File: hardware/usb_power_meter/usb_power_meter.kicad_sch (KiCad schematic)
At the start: 43 parts, among them J1 KH-1.27PH180-2X5P-L7.2-SMT, J2 917-P81A202ES60201, J4 A/F LCPTrue color1.2pillar_C4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, Q1 2N7002, Q2 IRML6401, SW1 TS-1187A-B-A-B, U1 nRF52833-QDxx, U2 INA226, X1 32Mhz crystal, X2 32.768kHz crystal

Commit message: Fix via sizes and 10k resistor footprint
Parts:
- R2, R3, R5, R6, R7: footprint Resistor_SMD:R_0201_0603Metric -> Resistor_SMD:R_0402_1005Metric; LCSC C25804 -> C270371
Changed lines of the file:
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@@
       (effects (font (size 1.27 1.27)) (justify left))
     )
-    (property "Footprint" "Resistor_SMD:R_0201_0603Metric" (at 139.7 137.668 90)
+    (property "Footprint" "Resistor_SMD:R_0402_1005Metric" (at 139.7 137.668 90)
       (effects (font (size 1.27 1.27)) hide)
     )
@@
       (effects (font (size 1.27 1.27)) hide)
     )
-    (property "LCSC" "C25804" (at 139.7 135.89 0)
+    (property "LCSC" "C270371" (at 139.7 135.89 0)
       (effects (font (size 1.27 1.27)) hide)
     )
@@
       (effects (font (size 1.27 1.27)) (justify left))
     )
-    (property "Footprint" "Resistor_SMD:R_0201_0603Metric" (at 144.78 147.828 90)
+    (property "Footprint" "Resistor_SMD:R_0402_1005Metric" (at 144.78 147.828 90)
       (effects (font (size 1.27 1.27)) hide)
     )
@@
       (effects (font (size 1.27 1.27)) hide)
     )
-    (property "LCSC" "C25804" (at 144.78 146.05 0)
+    (property "LCSC" "C270371" (at 144.78 146.05 0)
       (effects (font (size 1.27 1.27)) hide)
     )
@@
       (effects (font (size 1.27 1.27)) (justify left))
     )
-    (property "Footprint" "Resistor_SMD:R_0201_0603Metric" (at 75.692 181.61 90)
+    (property "Footprint" "Resistor_SMD:R_0402_1005Metric" (at 75.692 181.61 90)
       (effects (font (size 1.27 1.27)) hide)
     )
@@
       (effects (font (size 1.27 1.27)) hide)
     )
-    (property "LCSC" "C25804" (at 77.47 181.61 0)
+    (property "LCSC" "C270371" (at 77.47 181.61 0)
       (effects (font (size 1.27 1.27)) hide)
     )
@@
       (effects (font (size 1.27 1.27)) (justify left))
     )
-    (property "Footprint" "Resistor_SMD:R_0201_0603Metric" (at 92.202 167.64 90)
+    (property "Footprint" "Resistor_SMD:R_0402_1005Metric" (at 92.202 167.64 90)
       (effects (font (size 1.27 1.27)) hide)
     )
@@
       (effects (font (size 1.27 1.27)) hide)
     )
-    (property "LCSC" "C25804" (at 93.98 167.64 0)
+    (property "LCSC" "C270371" (at 93.98 167.64 0)
       (effects (font (size 1.27 1.27)) hide)
     )
@@
       (effects (font (size 1.27 1.27)) (justify left))
     )
-    (property "Footprint" "Resistor_SMD:R_0201_0603Metric" (at 142.24 142.748 90)
+    (property "Footprint" "Resistor_SMD:R_0402_1005Metric" (at 142.24 142.748 90)
       (effects (font (size 1.27 1.27)) hide)
     )
@@
       (effects (font (size 1.27 1.27)) hide)
     )
-    (property "LCSC" "C25804" (at 142.24 140.97 0)
-      (effects (font (size 1.27 1.27)) hide)
-    )
+    (property "LCSC" "C270371" (at 142.24 140.97 0)
+      (effects (font (size 1.27 1.27)) hide)
+    )

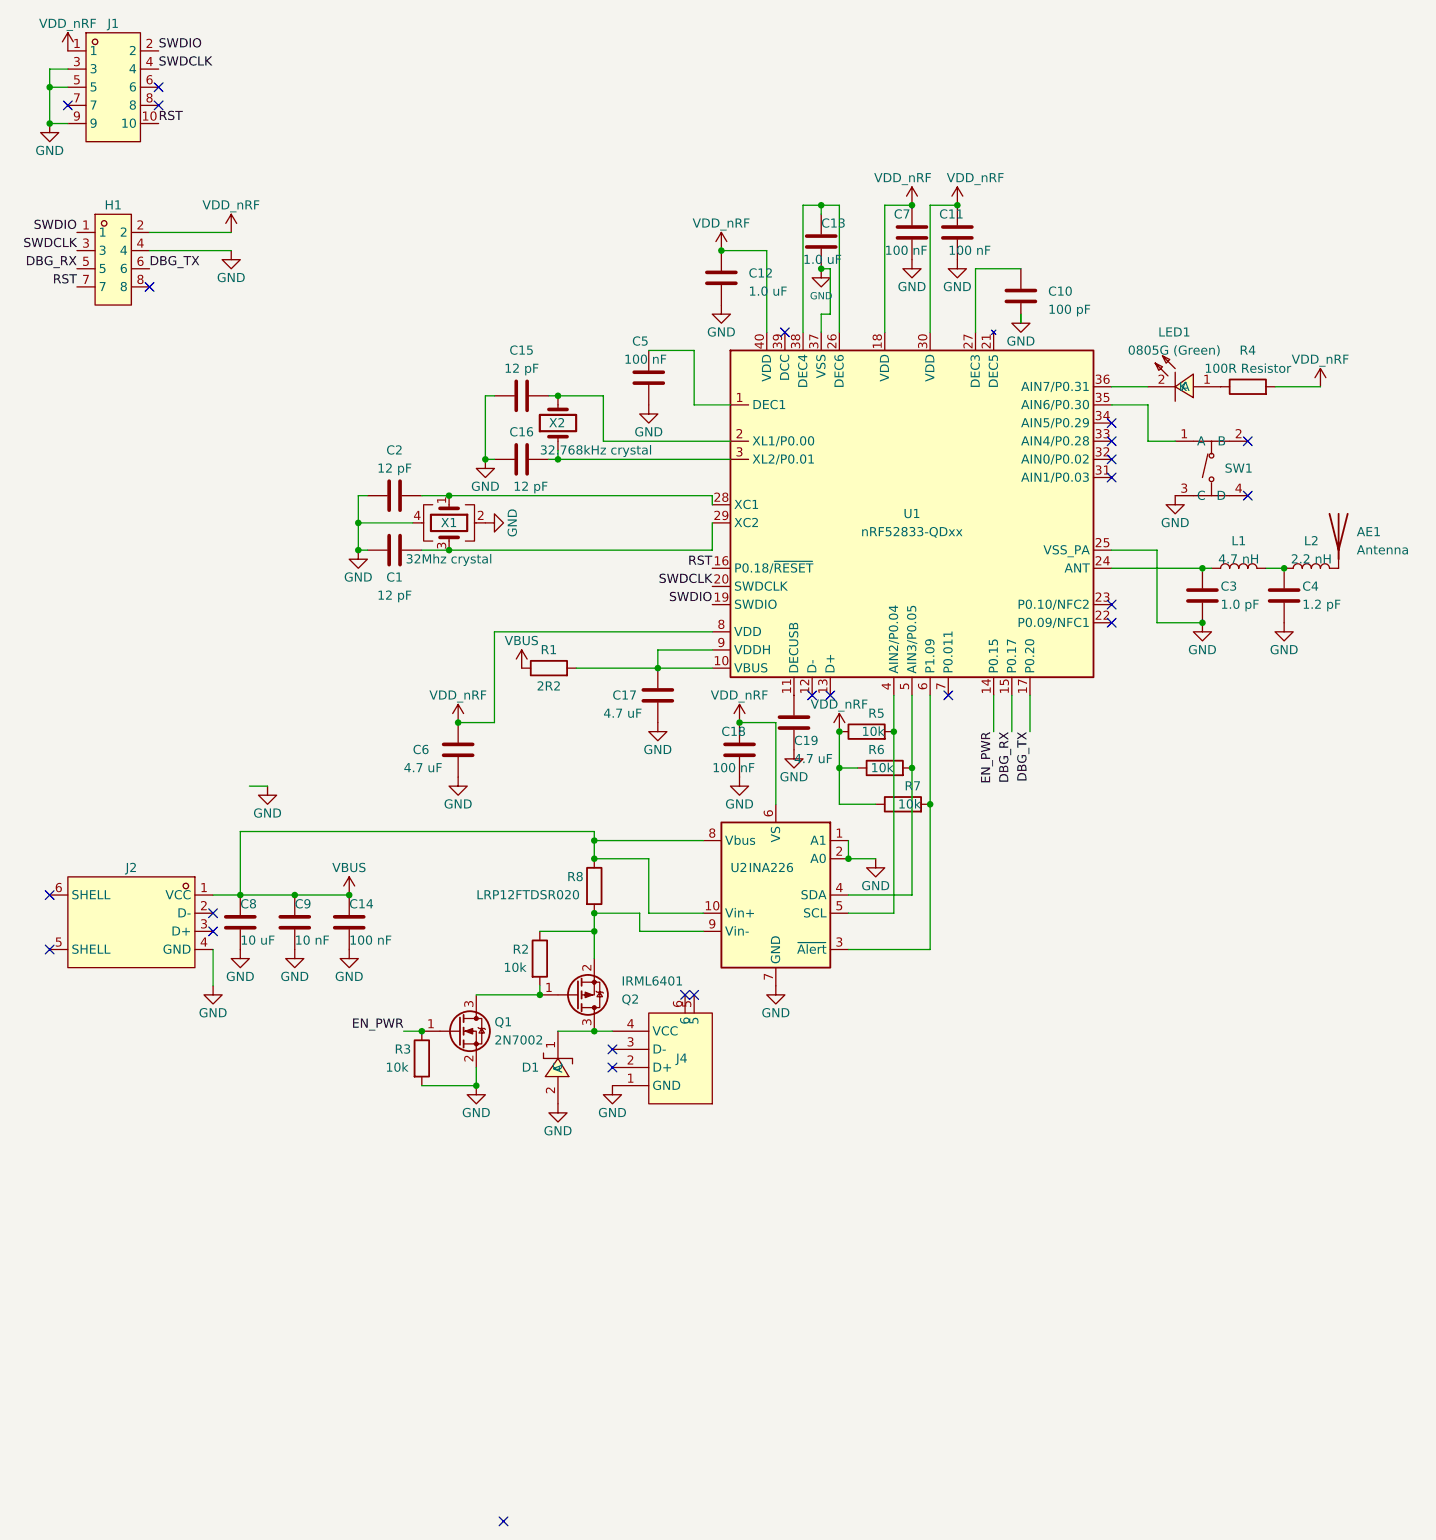
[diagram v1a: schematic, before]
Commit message: Update KiCad projects to the KiCad 8
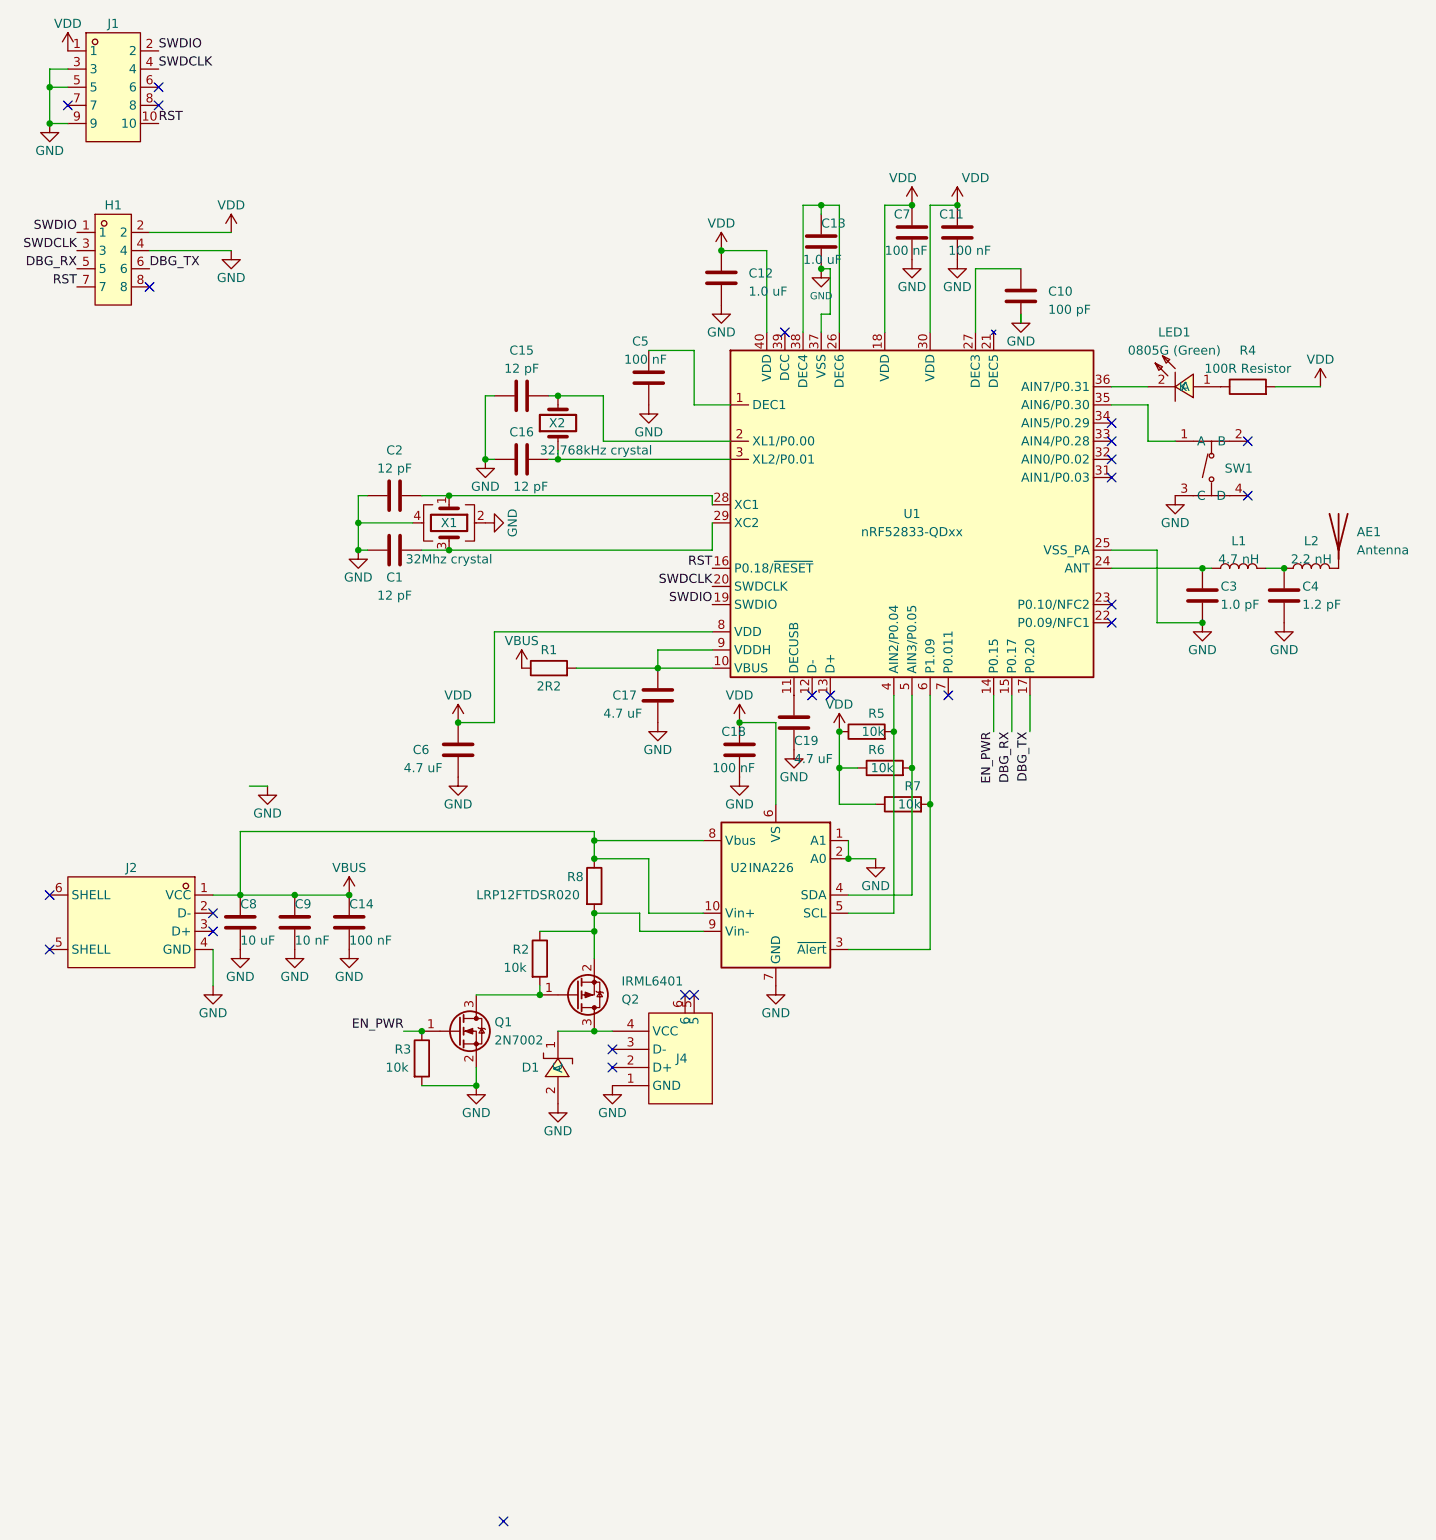
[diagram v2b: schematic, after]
